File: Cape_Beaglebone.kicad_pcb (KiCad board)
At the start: 2 copper layers, 79.4 x 54.6 mm, 92 parts, among them IC1 MPU-9250, IC10 HMC5883L-TR, IC11 BMP180, IC12 ADS8688IDBT, IC13 L3GD20H, IC2 HX711, IC3 DS3231S, IC4 HX711, IC5 CAT24C256WI-GT3, IC6 AD7793BRUZ, IC7 AD7793BRUZ, IC8 MPU-6500, IC9 LSM303D, J1 Conn_01x04, J10 Conn_01x04, J11 Conn_01x06, J12 Conn_01x04, J13 Conn_01x04, J14 Conn_01x04, J15 Conn_01x04, J16 Conn_01x06, J2 Conn_01x04, J3 Conn_01x02, J4 Conn_01x06, J5 M_WP, J6 Conn_01x06, J7 Conn_01x04, J8 Conn_01x04, J9 Conn_01x04, P8 BeagleBone_Black_Header, P9 BeagleBone_Black_Header, Q1 BC807, Q2 BC807, SW1 SW_DIP_x02, U1 4525DO-DS5AI001DP

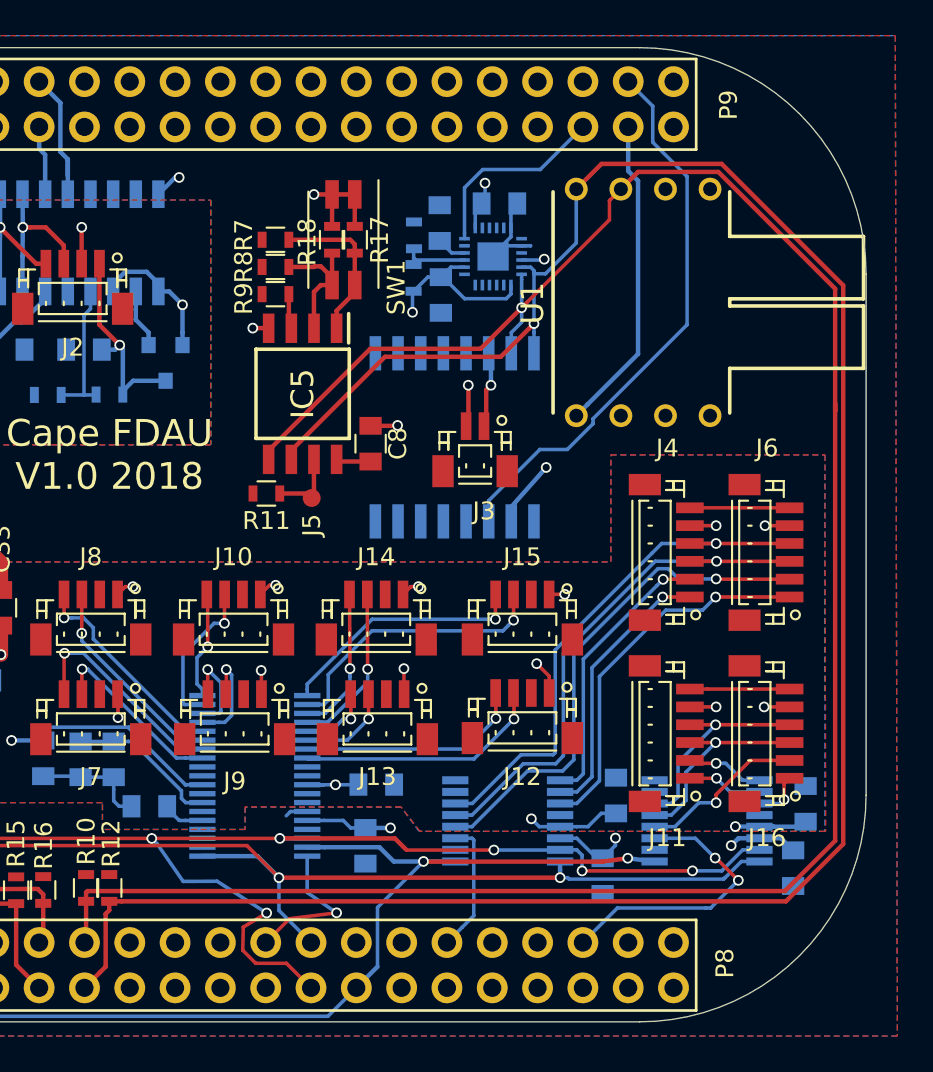
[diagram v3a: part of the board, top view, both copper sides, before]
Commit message: Corte para mangeira
Alteração para facilitar a colocação de magueira no sensor de pressão
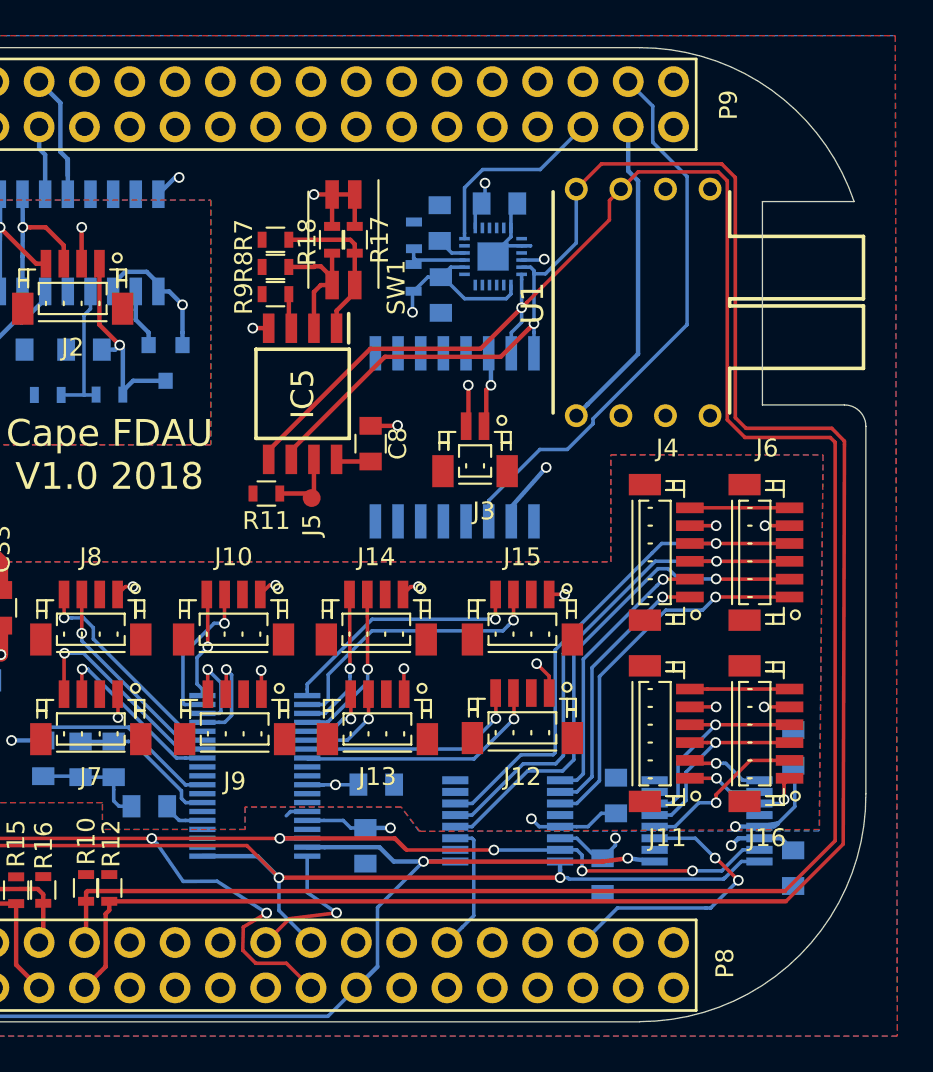
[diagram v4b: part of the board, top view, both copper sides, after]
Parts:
- moved C11 3.22 mm to (191.3, 86.4)
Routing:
- net SCL_I2C_2: track 126.1 -> 129.0 mm
- net SDA_I2C_2: track 124.1 -> 126.5 mm
- net +5VA: track 43.3 -> 44.8 mm
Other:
- outline, holes or cut-outs redrawn

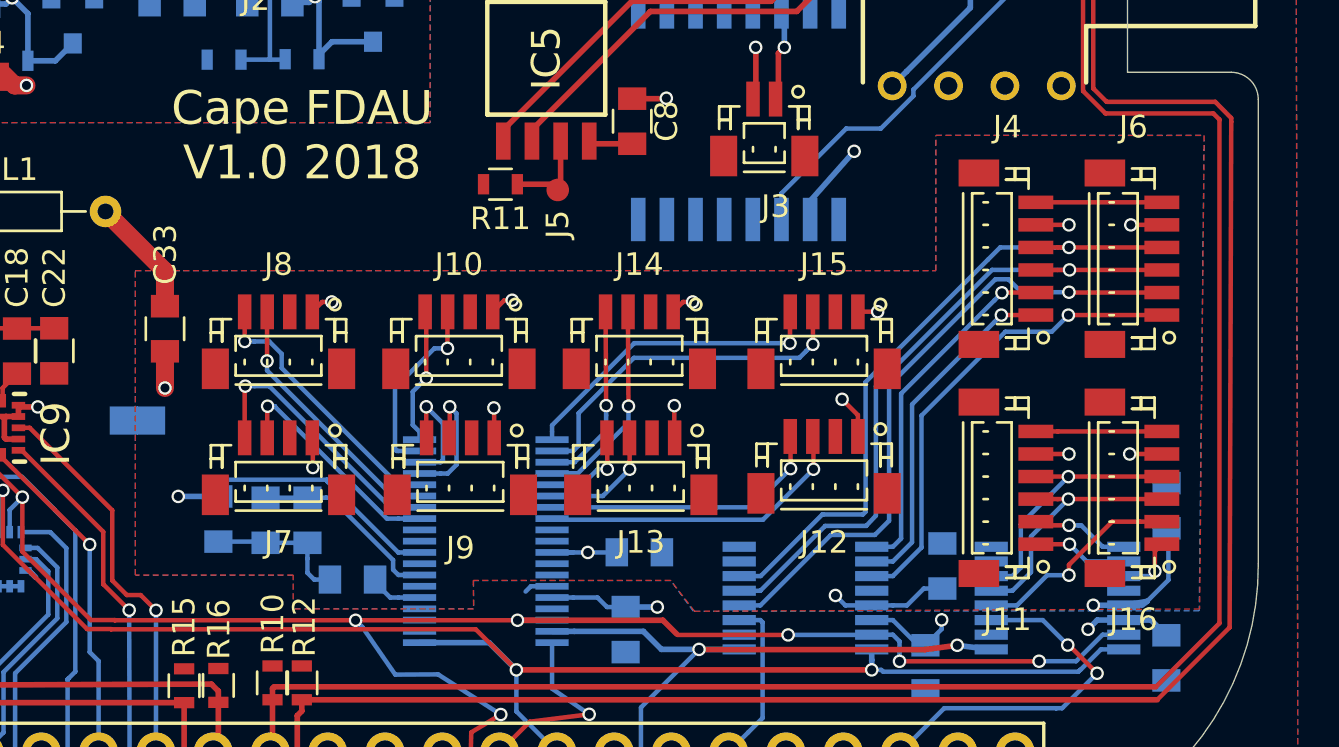
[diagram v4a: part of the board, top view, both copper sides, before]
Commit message: GNDA
Correções no ground
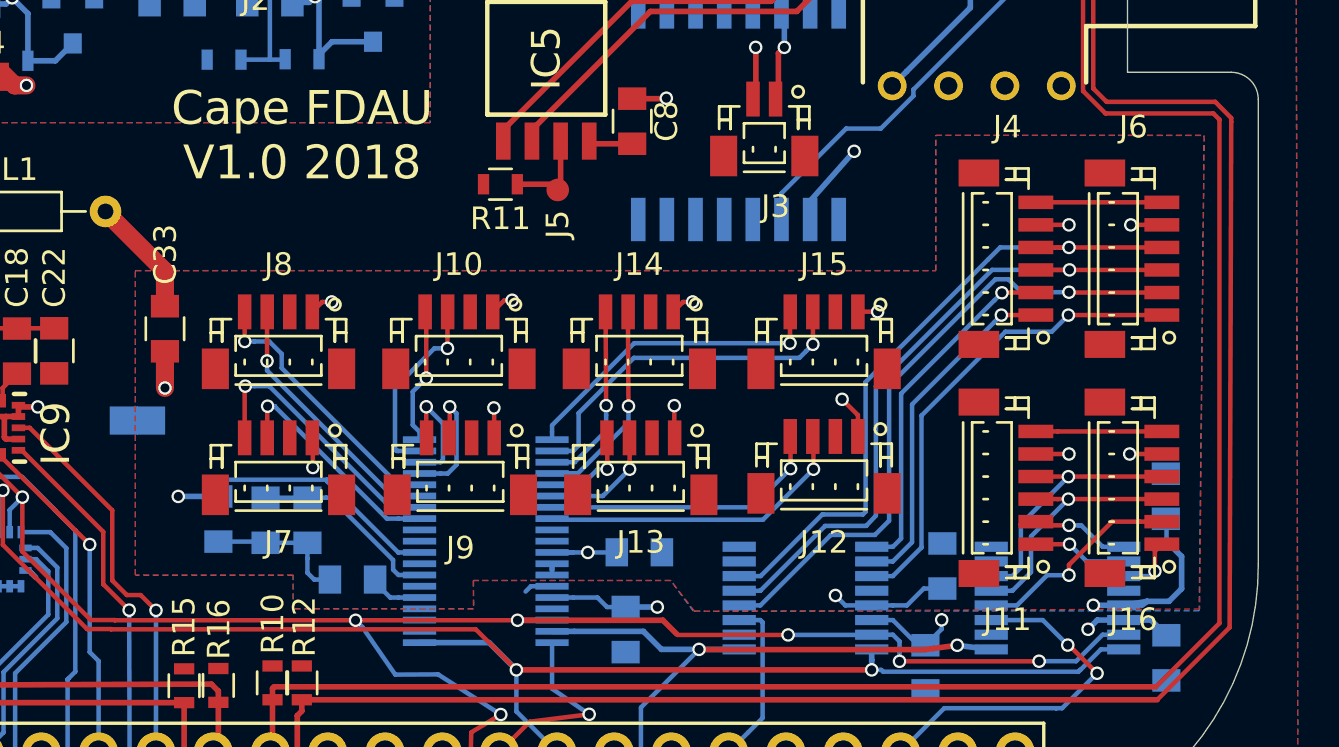
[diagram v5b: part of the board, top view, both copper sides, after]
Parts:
- moved C11 0.42 mm to (191.3, 86.0)
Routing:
- net +5VA: track 44.8 -> 45.8 mm
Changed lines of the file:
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@@
     (thickness 1.6)
     (drawings 17)
-    (tracks 999)
+    (tracks 1001)
     (zones 0)
     (modules 92)
@@
   (layers
     (0 F.Cu power)
-    (31 B.Cu signal)
+    (31 B.Cu signal hide)
     (33 F.Adhes user)
-    (35 F.Paste user)
+    (35 F.Paste user hide)
     (36 B.SilkS user)
     (37 F.SilkS user)
-    (38 B.Mask user)
+    (38 B.Mask user hide)
     (39 F.Mask user)
     (44 Edge.Cuts user)
-    (45 Margin user)
+    (45 Margin user hide)
     (46 B.CrtYd user)
     (47 F.CrtYd user)
   )
   (setup
-    (last_trace_width 0.2)
+    (last_trace_width 0.25)
     (user_trace_width 0.2)
     (user_trace_width 0.8)
@@
     (pad_to_mask_clearance 0)
     (aux_axis_origin 0 0)
-    (visible_elements 7FFFFF7F)
+    (visible_elements 7FFFFFFF)
     (pcbplotparams
       (layerselection 0x01030_ffffffff)
@@
   )
   (module Capacitors_SMD:C_0805 (layer B.Cu)
-    (at 191.33 86.42 90)
+    (at 191.3 86 90)
     (descr "Capacitor SMD 0805, reflow soldering, AVX (see smccp.pdf)")
     (tags "capacitor 0805")
@@
   (segment (start 154.233896 89.696104) (end 153.533896 89.696104) (width 0.2) (layer B.Cu) (net 18))
   (segment (start 146.917396 79.573104) (end 146.917396 81.198104) (width 0.8) (layer F.Cu) (net 18))
+  (segment (start 164.082296 88.992004) (end 164.082296 89.27499) (width 0.25) (layer B.Cu) (net 18))
   (segment (start 133.238896 63.275104) (end 133.937896 62.576104) (width 0.25) (layer B.Cu) (net 19))
   (segment (start 133.238896 64.150104) (end 133.238896 63.275104) (width 0.25) (layer B.Cu) (net 19))
@@
   (segment (start 177.091104 90.841104) (end 176.65 90.4) (width 0.2) (layer B.Cu) (net 25))
   (segment (start 178.257896 90.841104) (end 177.091104 90.841104) (width 0.2) (layer B.Cu) (net 25))
-  (segment (start 191.33 88.12) (end 191.413897 88.203897) (width 0.2) (layer B.Cu) (net 25))
-  (segment (start 191.33 87.42) (end 191.33 88.12) (width 0.2) (layer B.Cu) (net 25))
-  (segment (start 191.413897 89.713605) (end 190.467512 90.65999) (width 0.2) (layer B.Cu) (net 25))
-  (segment (start 191.413897 88.203897) (end 191.413897 89.713605) (width 0.2) (layer B.Cu) (net 25))
   (segment (start 189.433896 90.841104) (end 190.467512 90.65999) (width 0.25) (layer B.Cu) (net 25))
   (segment (start 190.467512 90.65999) (end 190.234896 90.841104) (width 0.25) (layer B.Cu) (net 25))
+  (segment (start 190.467512 90.65999) (end 191.44001 90.65999) (width 0.25) (layer B.Cu) (net 25))
+  (segment (start 191.44001 90.65999) (end 192 90.1) (width 0.25) (layer B.Cu) (net 25))
+  (segment (start 192 88.67) (end 191.33 88) (width 0.25) (layer B.Cu) (net 25))
+  (segment (start 192 90.1) (end 192 88.67) (width 0.25) (layer B.Cu) (net 25))
+  (segment (start 191.33 87.42) (end 191.33 88) (width 0.2) (layer B.Cu) (net 25))
   (segment (start 120.732396 95.675604) (end 121.529496 95.675604) (width 0.2) (layer B.Cu) (net 26))
   (segment (start 119.979896 94.923104) (end 120.732396 95.675604) (width 0.2) (layer B.Cu) (net 26))
@@
       (pts
         (xy 155.853896 90.746104) (xy 155.853896 90.996104) (xy 152.603896 90.996104) (xy 152.603896 89.496104) (xy 145.603896 89.496104)
-        (xy 145.603896 75.996104) (xy 181.103896 75.996104) (xy 181.103896 69.996104) (xy 193 70) (xy 192.846104 91.153896)
-        (xy 170.45 91.15) (xy 169.34 89.73) (xy 160.84 89.73) (xy 160.853896 90.996104) (xy 155.853896 90.996104)
-        (xy 155.853896 90.746104) (xy 159.353896 90.746104) (xy 160.353896 90.746104) (xy 160.34 89.61) (xy 169.34 89.61)
-        (xy 169.48 89.62) (xy 170.51 90.96) (xy 192.713896 91.006104) (xy 192.853896 70.246104) (xy 181.353896 70.246104)
-        (xy 181.353896 76.246104) (xy 145.853896 76.246104) (xy 145.853896 89.246104) (xy 152.853896 89.246104) (xy 152.853896 90.746104)
+        (xy 145.603896 75.996104) (xy 181.103896 75.996104) (xy 181.103896 69.996104) (xy 193 70) (xy 192.8 91.2)
+        (xy 170.403896 91.196104) (xy 169.4 89.8) (xy 160.9 89.8) (xy 160.853896 90.996104) (xy 155.853896 90.996104)
+        (xy 155.853896 90.746104) (xy 159.353896 90.746104) (xy 160.353896 90.746104) (xy 160.4 89.5) (xy 169.3 89.5)
+        (xy 169.6 89.5) (xy 170.6 90.9) (xy 192.5 91) (xy 192.7 70.4) (xy 181.5 70.4)
+        (xy 181.44 76.34) (xy 145.853896 76.246104) (xy 145.853896 89.246104) (xy 152.853896 89.246104) (xy 152.853896 90.746104)
       )
     )
@@
     (polygon
       (pts
-        (xy 145.603896 89.496104) (xy 145.603896 75.996104) (xy 181.103896 75.996104) (xy 181.103896 69.996104) (xy 193 70)
-        (xy 192.78 91.08) (xy 170.35 91.1) (xy 169.35 89.74) (xy 160.6 89.74) (xy 160.603896 90.996104)
-        (xy 152.603896 90.996104) (xy 152.603896 89.496104)
+        (xy 145.602466 89.494868) (xy 145.602466 75.994868) (xy 181.102466 75.994868) (xy 181.102466 69.994868) (xy 192.99857 69.998764)
+        (xy 192.77857 91.078764) (xy 170.34857 91.098764) (xy 169.34857 89.738764) (xy 160.59857 89.738764) (xy 160.602466 90.994868)
+        (xy 152.602466 90.994868) (xy 152.602466 89.494868)
       )
     )
